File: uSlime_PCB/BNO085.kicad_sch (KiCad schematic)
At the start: 9 parts, among them CN1 X1502WR-05K-N0SN, U5 BNO085

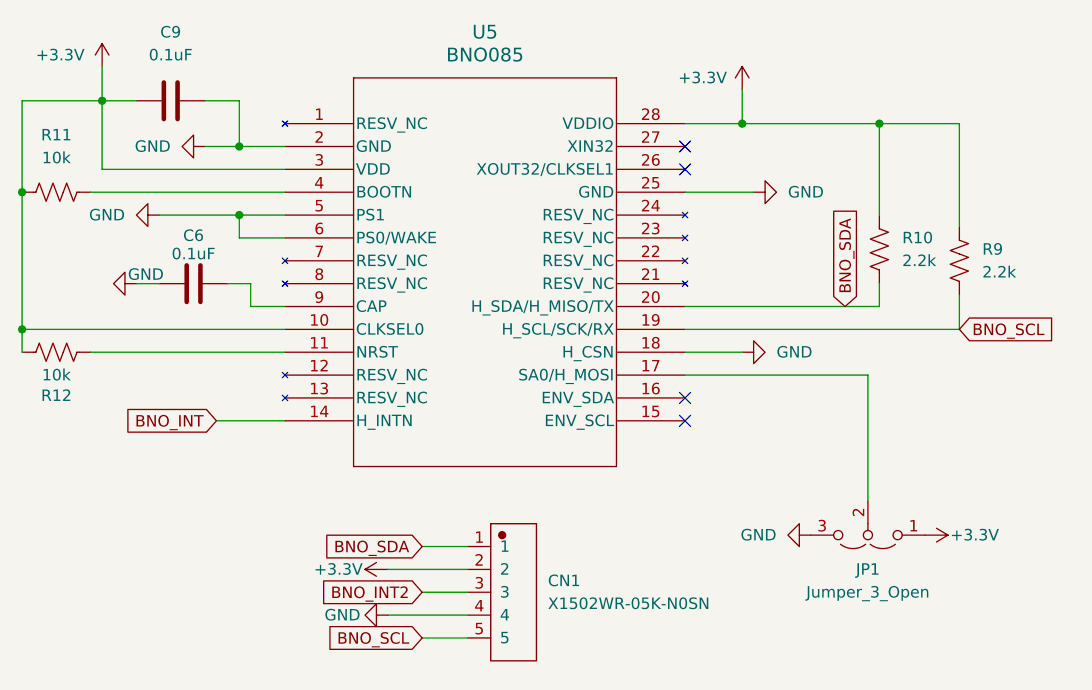
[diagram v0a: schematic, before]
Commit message: Connect pin 26 to GND
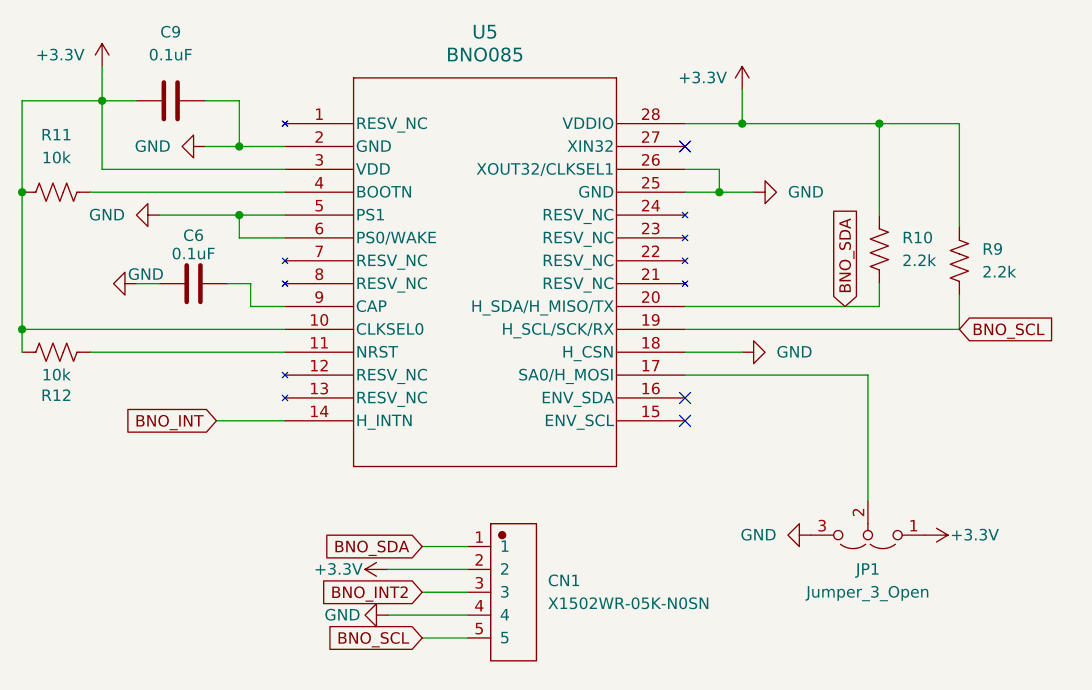
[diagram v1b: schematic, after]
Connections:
- net GND: now also U5.26 (XOUT32/CLKSEL1)
- no-connect marks 4 -> 3
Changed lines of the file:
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@@
+	)
+	(junction
+		(at 163.83 85.09)
+		(diameter 0)
+		(color 0 0 0 0)
 	)
 	(junction
@@
 		(diameter 0)
 		(color 0 0 0 0)
-	)
-	(no_connect
-		(at 160.02 82.55)
 	)
 	(no_connect
@@
 	(wire
 		(pts
+			(xy 163.83 85.09) (xy 160.02 85.09)
+		)
+		(stroke
+			(width 0)
+			(type default)
+		)
+	)
+	(wire
+		(pts
 			(xy 160.02 102.87) (xy 166.37 102.87)
 		)
@@
 	(wire
 		(pts
-			(xy 167.64 85.09) (xy 160.02 85.09)
+			(xy 167.64 85.09) (xy 163.83 85.09)
 		)
 		(stroke
@@
 	(wire
 		(pts
+			(xy 160.02 82.55) (xy 163.83 82.55)
+		)
+		(stroke
+			(width 0)
+			(type default)
+		)
+	)
+	(wire
+		(pts
 			(xy 110.49 87.63) (xy 110.49 90.17)
 		)
@@
 		)
 		(stroke
+			(width 0)
+			(type default)
+		)
+	)
+	(wire
+		(pts
+			(xy 163.83 82.55) (xy 163.83 85.09)
+		)
+		(stroke

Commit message: update schmetic
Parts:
- added R13: 10k, Resistor_SMD:R_0402_1005Metric, symbol uSlime:R_US
- added R14, R15: R_US, Resistor_SMD:R_0402_1005Metric, symbol uSlime:R_US
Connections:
- net +3.3V: now also R13.1, R14.2, R15.2
- net BNO_INT: now also R13.2
- net at U5.15 (ENV_SCL): now also R14.1
- net at U5.16 (ENV_SDA): now also R15.1
- no-connect marks 3 -> 1

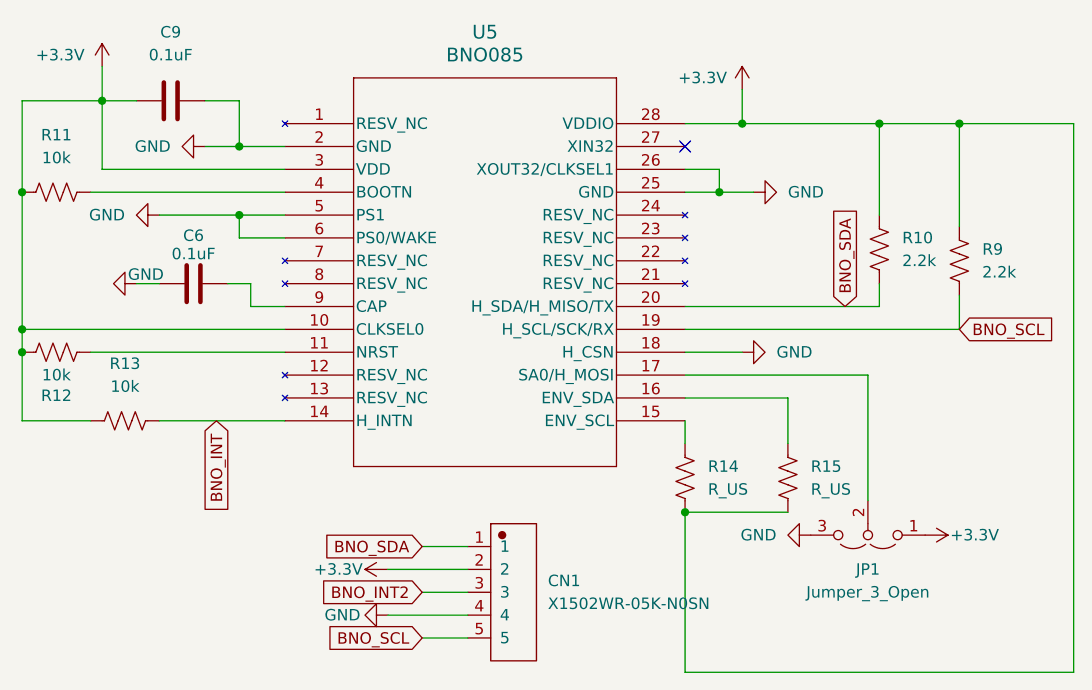
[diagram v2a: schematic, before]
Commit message: Modify PCB to add resistors to pins 14, 15, 16
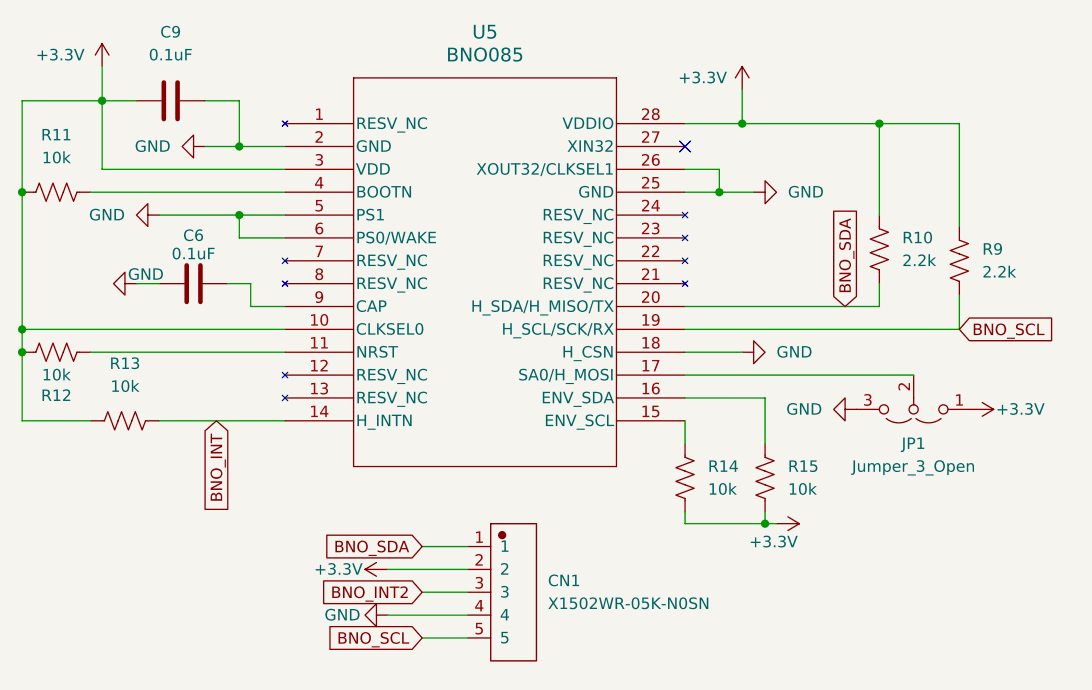
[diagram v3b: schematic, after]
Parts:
- R14, R15: value R_US -> 10k
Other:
- moved on the sheet: JP1, R15
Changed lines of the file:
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@@
-	)
-	(junction
-		(at 160.02 120.65)
-		(diameter 0)
-		(color 0 0 0 0)
 	)
 	(junction
@@
 	)
 	(junction
-		(at 190.5 77.47)
+		(at 168.91 121.92)
 		(diameter 0)
 		(color 0 0 0 0)
@@
 	(wire
 		(pts
-			(xy 203.2 77.47) (xy 190.5 77.47)
-		)
-		(stroke
-			(width 0)
-			(type default)
-		)
-	)
-	(wire
-		(pts
 			(xy 86.36 85.09) (xy 86.36 100.33)
 		)
@@
 	(wire
 		(pts
+			(xy 160.02 121.92) (xy 160.02 120.65)
+		)
+		(stroke
+			(width 0)
+			(type default)
+		)
+	)
+	(wire
+		(pts
 			(xy 160.02 102.87) (xy 166.37 102.87)
 		)
@@
 	(wire
 		(pts
-			(xy 160.02 120.65) (xy 160.02 138.43)
+			(xy 170.18 121.92) (xy 168.91 121.92)
 		)
 		(stroke
@@
 	(wire
 		(pts
-			(xy 180.34 105.41) (xy 180.34 119.38)
+			(xy 168.91 121.92) (xy 168.91 120.65)
 		)
 		(stroke
@@
 	(wire
 		(pts
-			(xy 160.02 107.95) (xy 171.45 107.95)
-		)
-		(stroke
-			(width 0)
-			(type default)
-		)
-	)
-	(wire
-		(pts
-			(xy 160.02 120.65) (xy 171.45 120.65)
+			(xy 160.02 107.95) (xy 168.91 107.95)
+		)
+		(stroke
+			(width 0)
+			(type default)
+		)
+	)
+	(wire
+		(pts
+			(xy 160.02 121.92) (xy 168.91 121.92)
 		)
 		(stroke
@@
 	(wire
 		(pts
-			(xy 160.02 138.43) (xy 203.2 138.43)
-		)
-		(stroke
-			(width 0)
-			(type default)
-		)
-	)
-	(wire
-		(pts
 			(xy 166.37 73.66) (xy 166.37 77.47)
 		)
@@
 	(wire
 		(pts
-			(xy 203.2 138.43) (xy 203.2 77.47)
-		)
-		(stroke
-			(width 0)
-			(type default)
-		)
-	)
-	(wire
-		(pts
 			(xy 95.25 82.55) (xy 115.57 82.55)
 		)
@@
 	(wire
 		(pts
-			(xy 171.45 107.95) (xy 171.45 113.03)
+			(xy 168.91 107.95) (xy 168.91 113.03)
 		)
 		(stroke
@@
 	(wire
 		(pts
-			(xy 160.02 105.41) (xy 180.34 105.41)
+			(xy 160.02 105.41) (xy 185.42 105.41)
 		)
 		(stroke
@@
 	(symbol
 		(lib_id "uSlime:Jumper_3_Open")
-		(at 180.34 123.19 180)
+		(at 185.42 109.22 180)
 		(unit 1)
 		(exclude_from_sim yes)
@@
 		(fields_autoplaced yes)
 		(property "Reference" "JP1"
-			(at 180.34 127 0)
+			(at 185.42 113.03 0)
 			(effects
 				(font
@@
 		)
 		(property "Value" "Jumper_3_Open"
-			(at 180.34 129.54 0)
+			(at 185.42 115.57 0)
 			(effects
 				(font
@@
 		)
 		(property "Footprint" "Jumper:SolderJumper-3_P1.3mm_Open_RoundedPad1.0x1.5mm"
-			(at 180.34 123.19 0)
+			(at 185.42 109.22 0)
 			(effects
 				(font
@@
 		)
 		(property "Datasheet" "~"
-			(at 180.34 123.19 0)
+			(at 185.42 109.22 0)
 			(effects
 				(font
@@
 		)
 		(property "Description" "Jumper, 3-pole, both open"
-			(at 180.34 123.19 0)
+			(at 185.42 109.22 0)
 			(effects
 				(font
@@
 	(symbol
 		(lib_id "power:GND")
-		(at 173.99 123.19 270)
+		(at 179.07 109.22 270)
 		(unit 1)
 		(exclude_from_sim no)
@@
 		(fields_autoplaced yes)
 		(property "Reference" "#PWR023"
-			(at 167.64 123.19 0)
+			(at 172.72 109.22 0)
 			(effects
 				(font
@@
 		)
 		(property "Value" "GND"
-			(at 170.18 123.1899 90)
+			(at 175.26 109.2199 90)
 			(effects
 				(font
@@
 		)
 		(property "Footprint" ""
-			(at 173.99 123.19 0)
+			(at 179.07 109.22 0)
 			(effects
 				(font
@@
 		)
 		(property "Datasheet" ""
-			(at 173.99 123.19 0)
+			(at 179.07 109.22 0)
 			(effects
 				(font
@@
 		)
 		(property "Description" "Power symbol creates a global label with name \"GND\" , ground"
-			(at 173.99 123.19 0)
+			(at 179.07 109.22 0)
 			(effects
 				(font
@@
 			)
 		)
-		(property "Value" "R_US"
+		(property "Value" "10k"
 			(at 162.56 118.1099 0)
 			(effects
@@
 	(symbol
 		(lib_id "power:+3.3V")
-		(at 186.69 123.19 270)
+		(at 191.77 109.22 270)
 		(unit 1)
 		(exclude_from_sim no)
@@
 		(dnp no)
 		(property "Reference" "#PWR024"
-			(at 182.88 123.19 0)
+			(at 187.96 109.22 0)
 			(effects
 				(font
@@
 		)
 		(property "Value" "+3.3V"
-			(at 189.484 123.19 90)
+			(at 194.564 109.22 90)
 			(effects
 				(font
@@
 		)
 		(property "Footprint" ""
-			(at 186.69 123.19 0)
+			(at 191.77 109.22 0)
 			(effects
 				(font
@@
 		)
 		(property "Datasheet" ""
-			(at 186.69 123.19 0)
+			(at 191.77 109.22 0)
 			(effects
 				(font
@@
 		)
 		(property "Description" "Power symbol creates a global label with name \"+3.3V\""
-			(at 186.69 123.19 0)
+			(at 191.77 109.22 0)
 			(effects
 				(font
@@
 	(symbol
 		(lib_id "uSlime:R_US")
-		(at 171.45 116.84 0)
+		(at 168.91 116.84 0)
 		(unit 1)
 		(exclude_from_sim no)
@@
 		(fields_autoplaced yes)
 		(property "Reference" "R15"
-			(at 173.99 115.5699 0)
+			(at 171.45 115.5699 0)
 			(effects
 				(font
@@
 			)
 		)
-		(property "Value" "R_US"
-			(at 173.99 118.1099 0)
+		(property "Value" "10k"
+			(at 171.45 118.1099 0)
 			(effects
 				(font
@@
 		)
 		(property "Footprint" "Resistor_SMD:R_0402_1005Metric"
-			(at 172.466 117.094 90)
+			(at 169.926 117.094 90)
 			(effects
 				(font
@@
 		)
 		(property "Datasheet" "~"
-			(at 171.45 116.84 0)
+			(at 168.91 116.84 0)
 			(effects
 				(font
@@
 		)
 		(property "Description" "Resistor, US symbol"
-			(at 171.45 116.84 0)
+			(at 168.91 116.84 0)
 			(effects
 				(font
@@
 					(unit 1)
 				)
+			)
+		)
+	)
+	(symbol
+		(lib_id "power:+3.3V")
+		(at 170.18 121.92 270)
+		(unit 1)
+		(exclude_from_sim no)
+		(in_bom yes)
+		(on_board yes)
+		(dnp no)
+		(property "Reference" "#PWR011"
+			(at 166.37 121.92 0)
+			(effects
+				(font
+					(size 1.27 1.27)
+				)
+				(hide yes)
+			)
+		)
+		(property "Value" "+3.3V"
+			(at 167.132 123.952 90)
+			(effects
+				(font
+					(size 1.27 1.27)
+				)
+				(justify left)
+			)
+		)
+		(property "Footprint" ""
+			(at 170.18 121.92 0)
+			(effects
+				(font
+					(size 1.27 1.27)
+				)
+				(hide yes)
+			)
+		)
+		(property "Datasheet" ""
+			(at 170.18 121.92 0)
+			(effects
+				(font
+					(size 1.27 1.27)
+				)
+				(hide yes)
+			)
+		)
+		(property "Description" "Power symbol creates a global label with name \"+3.3V\""
+			(at 170.18 121.92 0)
+			(effects
+				(font
+					(size 1.27 1.27)
+				)
+				(hide yes)
+			)
+		)
+		(pin "1"
+		)
+		(instances
+			(project "uSlime"
+				(path "/f32c1c49-f803-4e7c-a530-6db148a7ba36/1072de81-ddaf-4115-9b1e-8b480e2a0117"
+					(reference "#PWR011")
+					(unit 1)
+				)

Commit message: Remove GPIO9 capacitor causing boot problems
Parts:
- renumbered C6 to C1, C9 to C2, CN1 to CN2, R9 to R10, R10 to R11, R12 to R13, R13 to R14, R14 to R15, R11 to R5, R15 to R7
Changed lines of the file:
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@@
 		(on_board yes)
 		(dnp no)
-		(property "Reference" "R12"
+		(property "Reference" "R13"
 			(at 90.17 107.696 90)
 			(effects
@@
 			(project "uSlime"
 				(path "/f32c1c49-f803-4e7c-a530-6db148a7ba36/1072de81-ddaf-4115-9b1e-8b480e2a0117"
-					(reference "R12")
+					(reference "R13")
 					(unit 1)
 				)
@@
 		(on_board yes)
 		(dnp no)
-		(property "Reference" "C6"
+		(property "Reference" "C1"
 			(at 105.41 89.916 90)
 			(effects
@@
 			(project "uSlime"
 				(path "/f32c1c49-f803-4e7c-a530-6db148a7ba36/1072de81-ddaf-4115-9b1e-8b480e2a0117"
-					(reference "C6")
+					(reference "C1")
 					(unit 1)
 				)
@@
 		(dnp no)
 		(fields_autoplaced yes)
-		(property "Reference" "R13"
+		(property "Reference" "R14"
 			(at 97.79 104.14 90)
 			(effects
@@
 			(project "uSlime"
 				(path "/f32c1c49-f803-4e7c-a530-6db148a7ba36/1072de81-ddaf-4115-9b1e-8b480e2a0117"
-					(reference "R13")
+					(reference "R14")
 					(unit 1)
 				)
@@
 		(dnp no)
 		(fields_autoplaced yes)
-		(property "Reference" "R11"
+		(property "Reference" "R5"
 			(at 90.17 78.74 90)
 			(effects
@@
 			(project "uSlime"
 				(path "/f32c1c49-f803-4e7c-a530-6db148a7ba36/1072de81-ddaf-4115-9b1e-8b480e2a0117"
-					(reference "R11")
+					(reference "R5")
 					(unit 1)
 				)
@@
 		(dnp no)
 		(fields_autoplaced yes)
-		(property "Reference" "R14"
+		(property "Reference" "R15"
 			(at 162.56 115.5699 0)
 			(effects
@@
 			(project "uSlime"
 				(path "/f32c1c49-f803-4e7c-a530-6db148a7ba36/1072de81-ddaf-4115-9b1e-8b480e2a0117"
-					(reference "R14")
+					(reference "R15")
 					(unit 1)
 				)
@@
 		(dnp no)
 		(fields_autoplaced yes)
-		(property "Reference" "R9"
+		(property "Reference" "R10"
 			(at 193.04 91.4399 0)
 			(effects
@@
 			(project "uSlime"
 				(path "/f32c1c49-f803-4e7c-a530-6db148a7ba36/1072de81-ddaf-4115-9b1e-8b480e2a0117"
-					(reference "R9")
+					(reference "R10")
 					(unit 1)
 				)
@@
 		(dnp no)
 		(fields_autoplaced yes)
-		(property "Reference" "R10"
+		(property "Reference" "R11"
 			(at 184.15 90.1699 0)
 			(effects
@@
 			(project "uSlime"
 				(path "/f32c1c49-f803-4e7c-a530-6db148a7ba36/1072de81-ddaf-4115-9b1e-8b480e2a0117"
-					(reference "R10")
+					(reference "R11")
 					(unit 1)
 				)
@@
 		(dnp no)
 		(fields_autoplaced yes)
-		(property "Reference" "CN1"
+		(property "Reference" "CN2"
 			(at 144.78 128.2699 0)
 			(effects
@@
 			(project "uSlime"
 				(path "/f32c1c49-f803-4e7c-a530-6db148a7ba36/1072de81-ddaf-4115-9b1e-8b480e2a0117"
-					(reference "CN1")
+					(reference "CN2")
 					(unit 1)
 				)
@@
 		(dnp no)
 		(fields_autoplaced yes)
-		(property "Reference" "R15"
+		(property "Reference" "R7"
 			(at 171.45 115.5699 0)
 			(effects
@@
 			(project "uSlime"
 				(path "/f32c1c49-f803-4e7c-a530-6db148a7ba36/1072de81-ddaf-4115-9b1e-8b480e2a0117"
-					(reference "R15")
+					(reference "R7")
 					(unit 1)
 				)
@@
 		(dnp no)
 		(fields_autoplaced yes)
-		(property "Reference" "C9"
+		(property "Reference" "C2"
 			(at 102.87 67.31 90)
 			(effects
@@
 			(project "uSlime"
 				(path "/f32c1c49-f803-4e7c-a530-6db148a7ba36/1072de81-ddaf-4115-9b1e-8b480e2a0117"
-					(reference "C9")
-					(unit 1)
-				)
+					(reference "C2")
+					(unit 1)
+				)
